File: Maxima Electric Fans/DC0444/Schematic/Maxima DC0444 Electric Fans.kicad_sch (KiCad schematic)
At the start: 2 parts, among them M1 Fan_Maxima, M2 Fan_Maxima

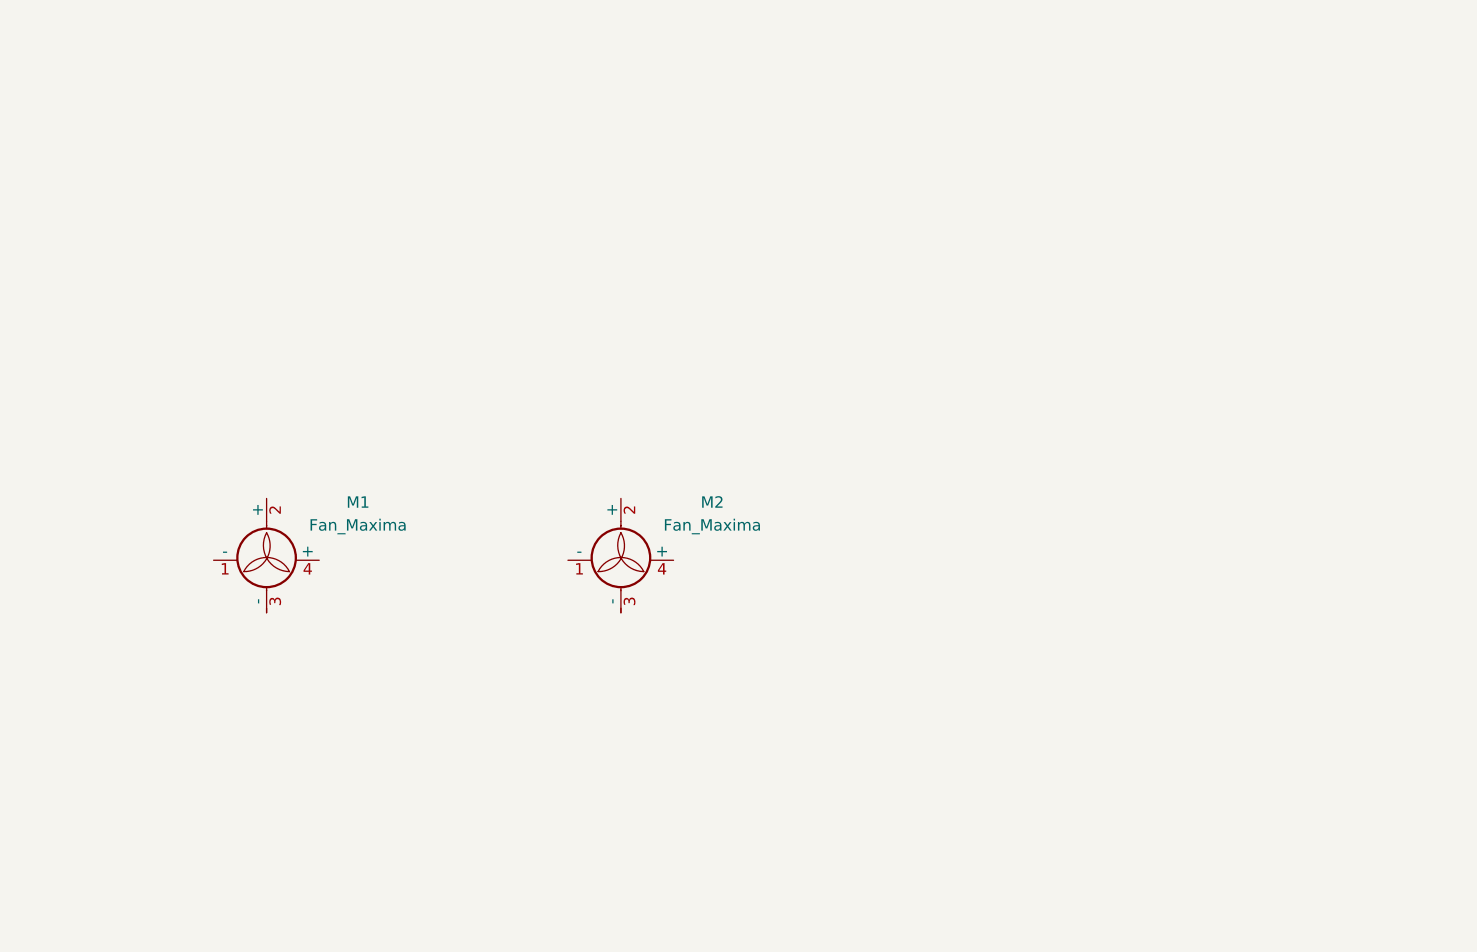
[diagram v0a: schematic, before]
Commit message: Complete DC0444 Maxima fan controller design
Finish the DC0444 schematic, add the MaximaFans symbol library and
sym-lib-table, and include the rendered JPG/PDF of the design.

Also ignore *.bak so KiCad's symbol-library backups stop landing in
commits (the existing *.kicad_sym.bak pattern didn't match KiCad's
real <name>.bak naming).
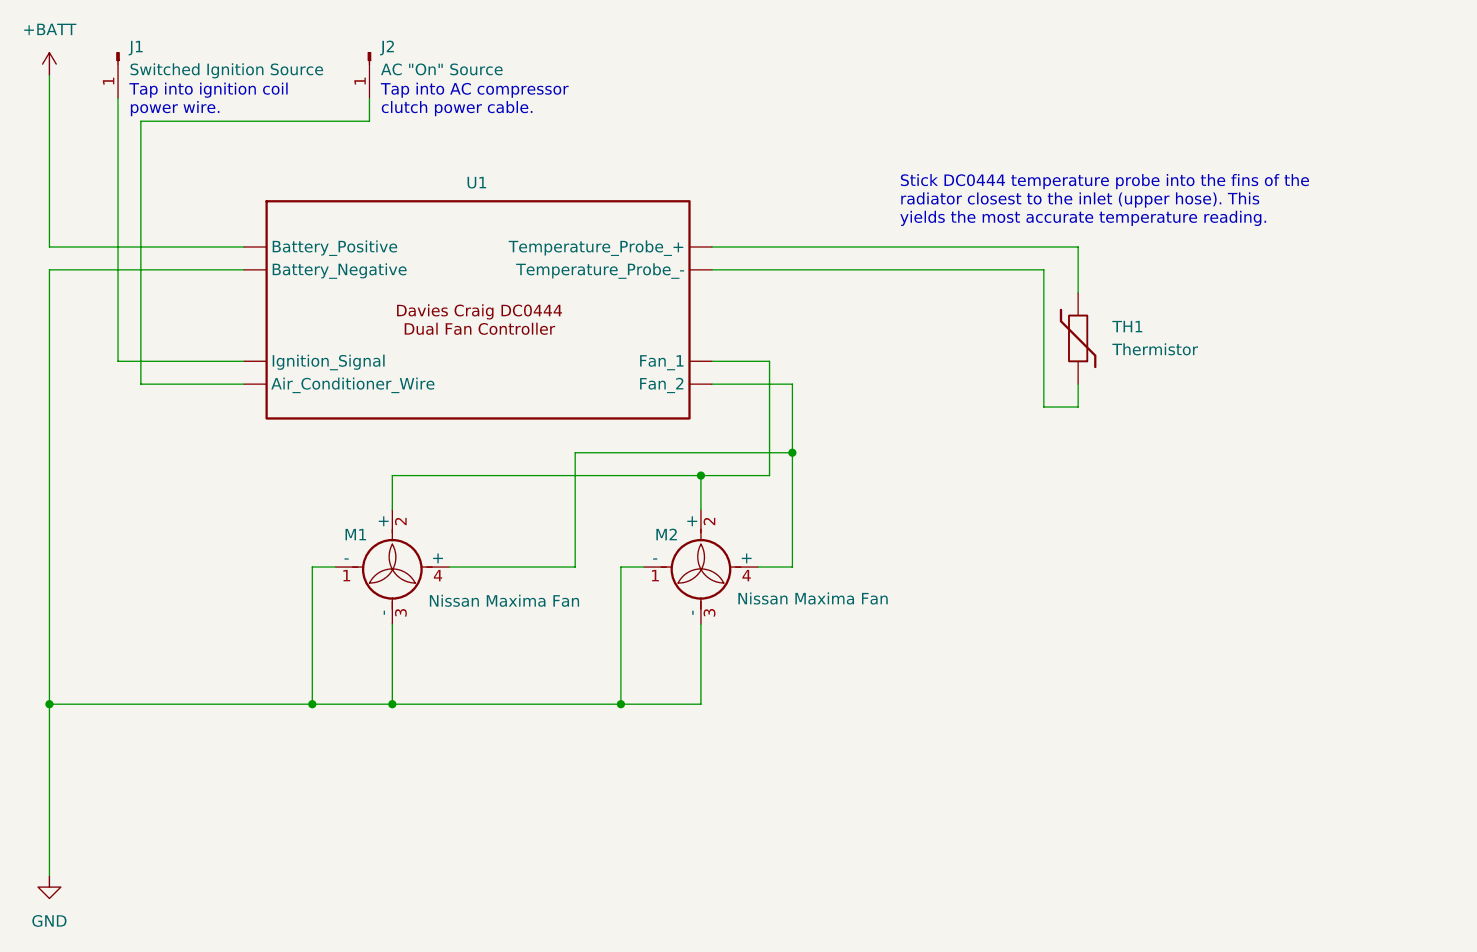
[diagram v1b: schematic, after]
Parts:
- removed M1, M2: Fan_Maxima, symbol Motor:Fan_Maxima
- added J1: Switched Ignition Source, symbol Connector:Conn_01x01_Pin
- added J2: AC "On" Source, symbol Connector:Conn_01x01_Pin
- added M1, M2: Nissan Maxima Fan, symbol MaximaFans:Fan_Maxima
- added TH1: Thermistor, symbol Device:Thermistor
- added U1: ~, symbol MaximaFans:Fan_Controller_DC0444
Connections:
- new net: J1.1 (Pin_1), U1. (Fan_2)
- new net: TH1.1, U1. (Fan_2)
- new net: TH1.2, U1. (Fan_2)
- new net: M1.2 (+), M2.2 (+), U1. (Fan_2)
- new net: M1.4 (+), M2.4 (+), U1. (Fan_2)
- new net: J2.1 (Pin_1), U1. (Fan_2)
- new net +BATT: U1. (Fan_2)
- new net GND: M1.1 (-), M1.3 (-), M2.1 (-), M2.3 (-), U1. (Fan_2)
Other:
- note added: "Stick DC0444 temperature probe into the fins of the radiator closest to the inlet (upper hose). This yields the most accurate temperature reading."
- note added: "Tap into AC compressor clutch power cable."
- note added: "Tap into ignition coil power wire."
- title: (none) -> Nissan Maxima DC0444 Fan Wiring
